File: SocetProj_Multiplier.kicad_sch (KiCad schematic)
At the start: 23 parts, among them J1 Barrel_Jack, U1 74LS283, U2 74LS283, U4 74LS86, U5 74LS86

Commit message: Finished schematic, need to look at power output of the mux potentially to drive LED pins, otherwise logic SHOULD be done
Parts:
- added C32, C33: .1u, symbol Device:C
- added Input_A, Input_B: Conn_01x09_Pin, symbol Connector:Conn_01x09_Pin
- added Outputs: Conn_01x17_Pin, symbol Connector:Conn_01x17_Pin
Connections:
- net +5V: now also U4.14 (VCC), U5.14 (VCC), C32.1, C33.1
- net A0: now also Input_A.1 (Pin_1)
- net A1: now also Input_A.2 (Pin_2)
- net A2: now also Input_A.3 (Pin_3)
- net A3: now also Input_A.4 (Pin_4)
- net A4: now also Input_A.5 (Pin_5)
- net A5: now also Input_A.6 (Pin_6)
- net A6: now also Input_A.7 (Pin_7)
- net A7: now also Input_A.8 (Pin_8)
- net B0: now also Input_B.1 (Pin_1)
- net B1: now also Input_B.2 (Pin_2)
- net B2: now also Input_B.3 (Pin_3)
- net B3: now also Input_B.4 (Pin_4)
- net B4: now also Input_B.5 (Pin_5)
- net B5: now also Input_B.6 (Pin_6)
- net B6: now also Input_B.7 (Pin_7)
- net B7: now also Input_B.8 (Pin_8)
- net GND: now also C32.2, C33.2, Input_A.9 (Pin_9), Input_B.9 (Pin_9), Outputs.17 (Pin_17)
- net Add1: now reaches U1.1 (S2)
- net Add3: now reaches U1.10 (S4)
- net Add2: now reaches U1.13 (S3)
- net Add0: now reaches U1.4 (S1)
- net Add5: now reaches U2.1 (S2)
- net Add7: now reaches U2.10 (S4)
- net Add6: now reaches U2.13 (S3)
- net Add4: now reaches U2.4 (S1)
- net Add8: now reaches U2.9 (C4)
- new net Z0: Outputs.1 (Pin_1)
- new net Z1: Outputs.2 (Pin_2)
- new net Z10: Outputs.11 (Pin_11)
- new net Z11: Outputs.12 (Pin_12)
- new net Z12: Outputs.13 (Pin_13)
- new net Z13: Outputs.14 (Pin_14)
- new net Z14: Outputs.15 (Pin_15)
- new net Z15: Outputs.16 (Pin_16)
- new net Z2: Outputs.3 (Pin_3)
- new net Z3: Outputs.4 (Pin_4)
- new net Z4: Outputs.5 (Pin_5)
- new net Z5: Outputs.6 (Pin_6)
- new net Z6: Outputs.7 (Pin_7)
- new net Z7: Outputs.8 (Pin_8)
- new net Z8: Outputs.9 (Pin_9)
- new net Z9: Outputs.10 (Pin_10)
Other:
- added sheet MUX (Mux.kicad_sch)
- sheet Dadda_Multiplier ports: added F0, F1, F10, F11, F12, F13, F14, F15, F2, F3, F4, F5, F6, F7, F8, F9; removed none

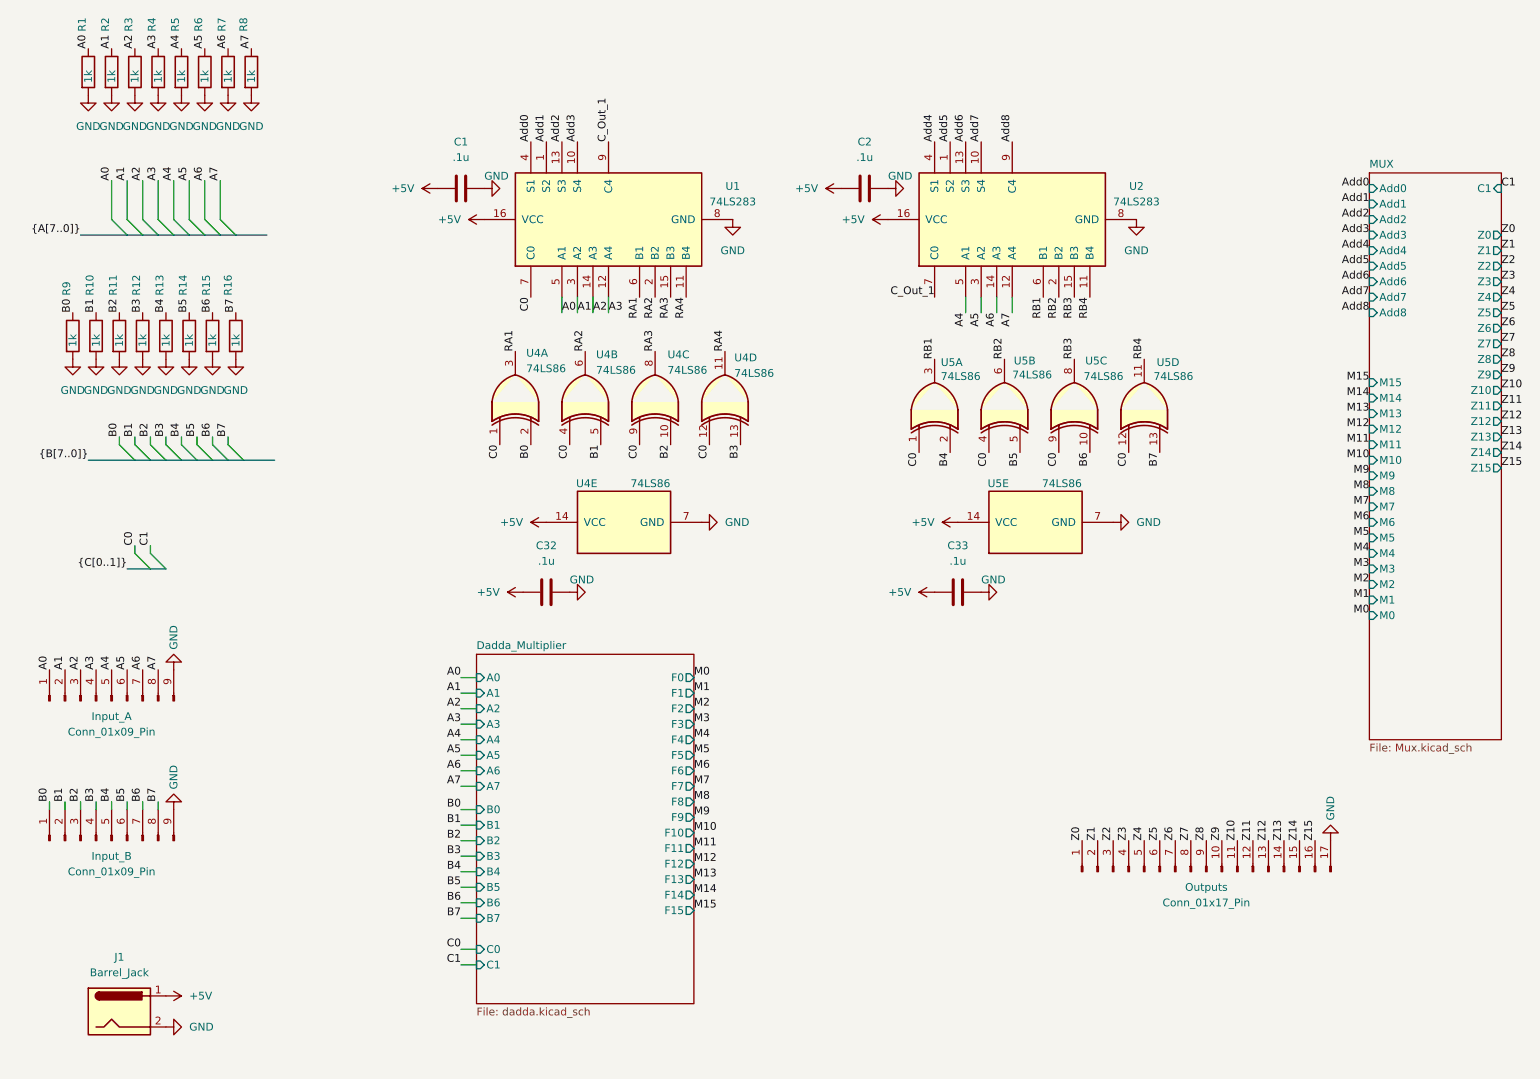
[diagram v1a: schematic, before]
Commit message: Fixed ERC issues and applied Footprints
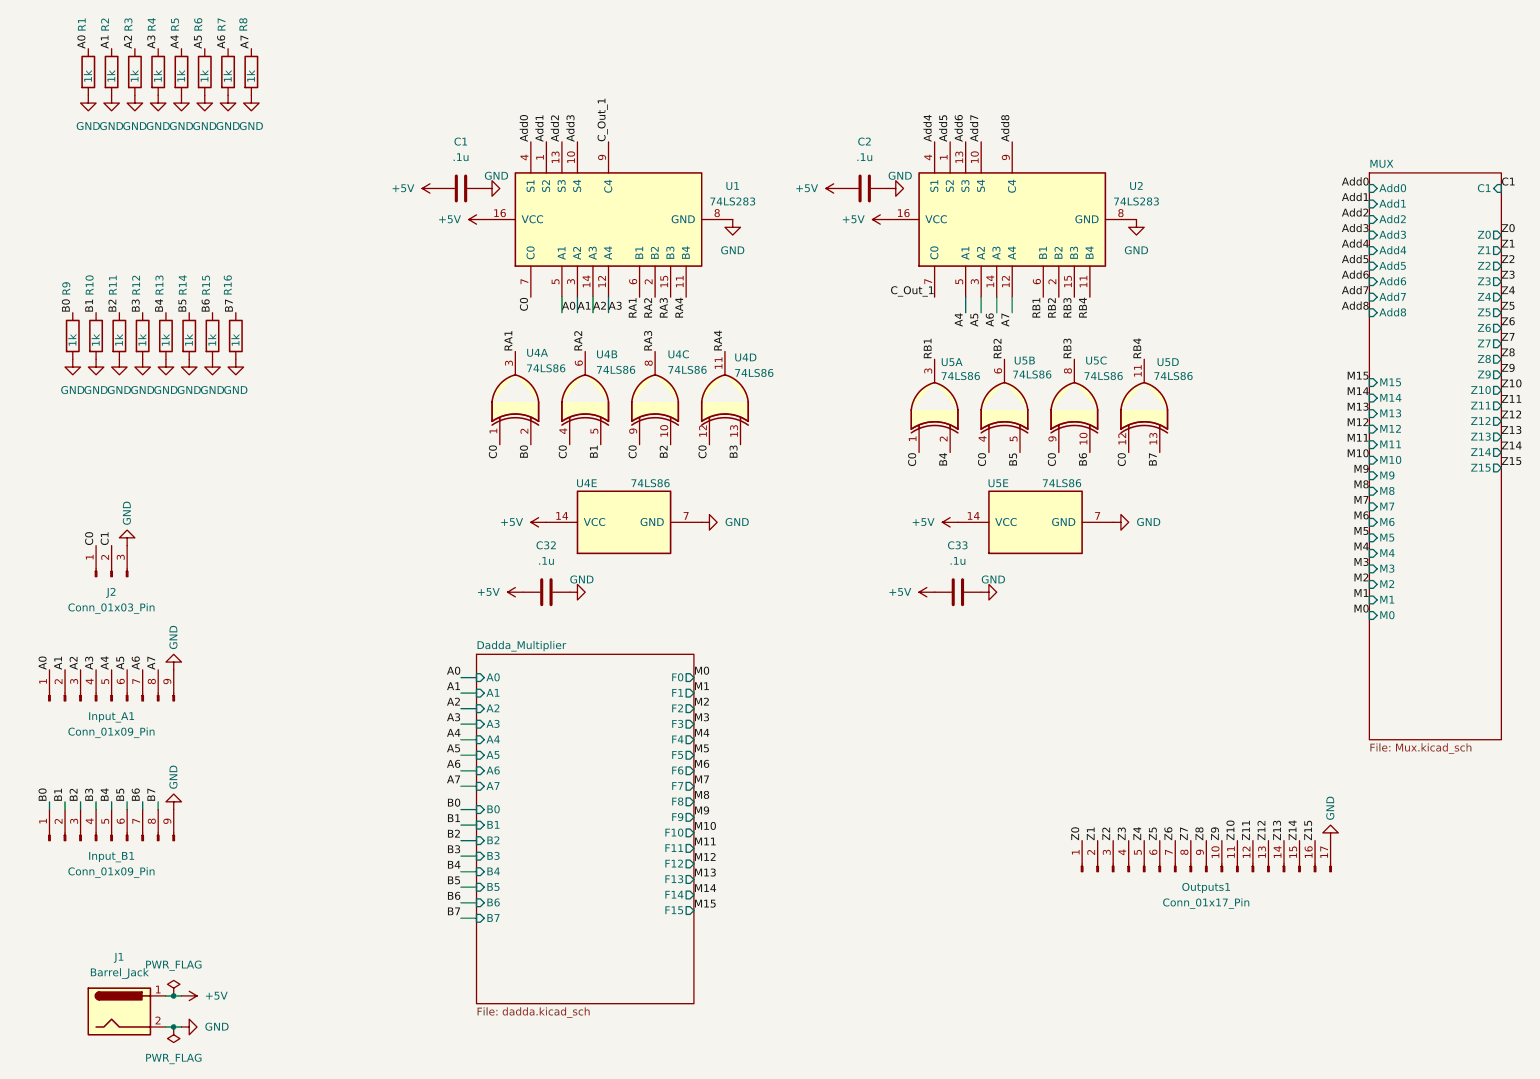
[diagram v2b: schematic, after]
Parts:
- added J2: Conn_01x03_Pin, Connector_PinHeader_2.54mm:PinHeader_1x03_P2.54mm_Vertical, symbol Connector:Conn_01x03_Pin
- C1, C2, C32, C33: footprint (none) -> Capacitor_SMD:C_0402_1005Metric
- Input_A1: renamed from Input_A; footprint (none) -> Connector_PinHeader_2.54mm:PinHeader_1x09_P2.54mm_Vertical
- Input_B1: renamed from Input_B; footprint (none) -> Connector_PinHeader_2.54mm:PinHeader_1x09_P2.54mm_Vertical
- Outputs1: renamed from Outputs; footprint (none) -> Connector_PinHeader_2.54mm:PinHeader_1x17_P2.54mm_Vertical
- R1, R10, R11, R12, R13, R14, R15, R16, R2, R3, R4, R5, R6, R7, R8, R9: footprint (none) -> Resistor_SMD:R_0402_1005Metric
- U1, U2: footprint (none) -> Package_SO:SOIC-16_3.9x9.9mm_P1.27mm
- U4, U5: footprint (none) -> Package_SO:SOIC-14-16_3.9x9.9mm_P1.27mm
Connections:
- net C0: now also J2.1 (Pin_1)
- net C1: now also J2.2 (Pin_2)
- net GND: now also J2.3 (Pin_3)
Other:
- sheet Dadda_Multiplier ports: added none; removed C0, C1
